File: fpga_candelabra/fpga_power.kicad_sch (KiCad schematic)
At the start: 1 part, among them U1 XCVU13P-B2104

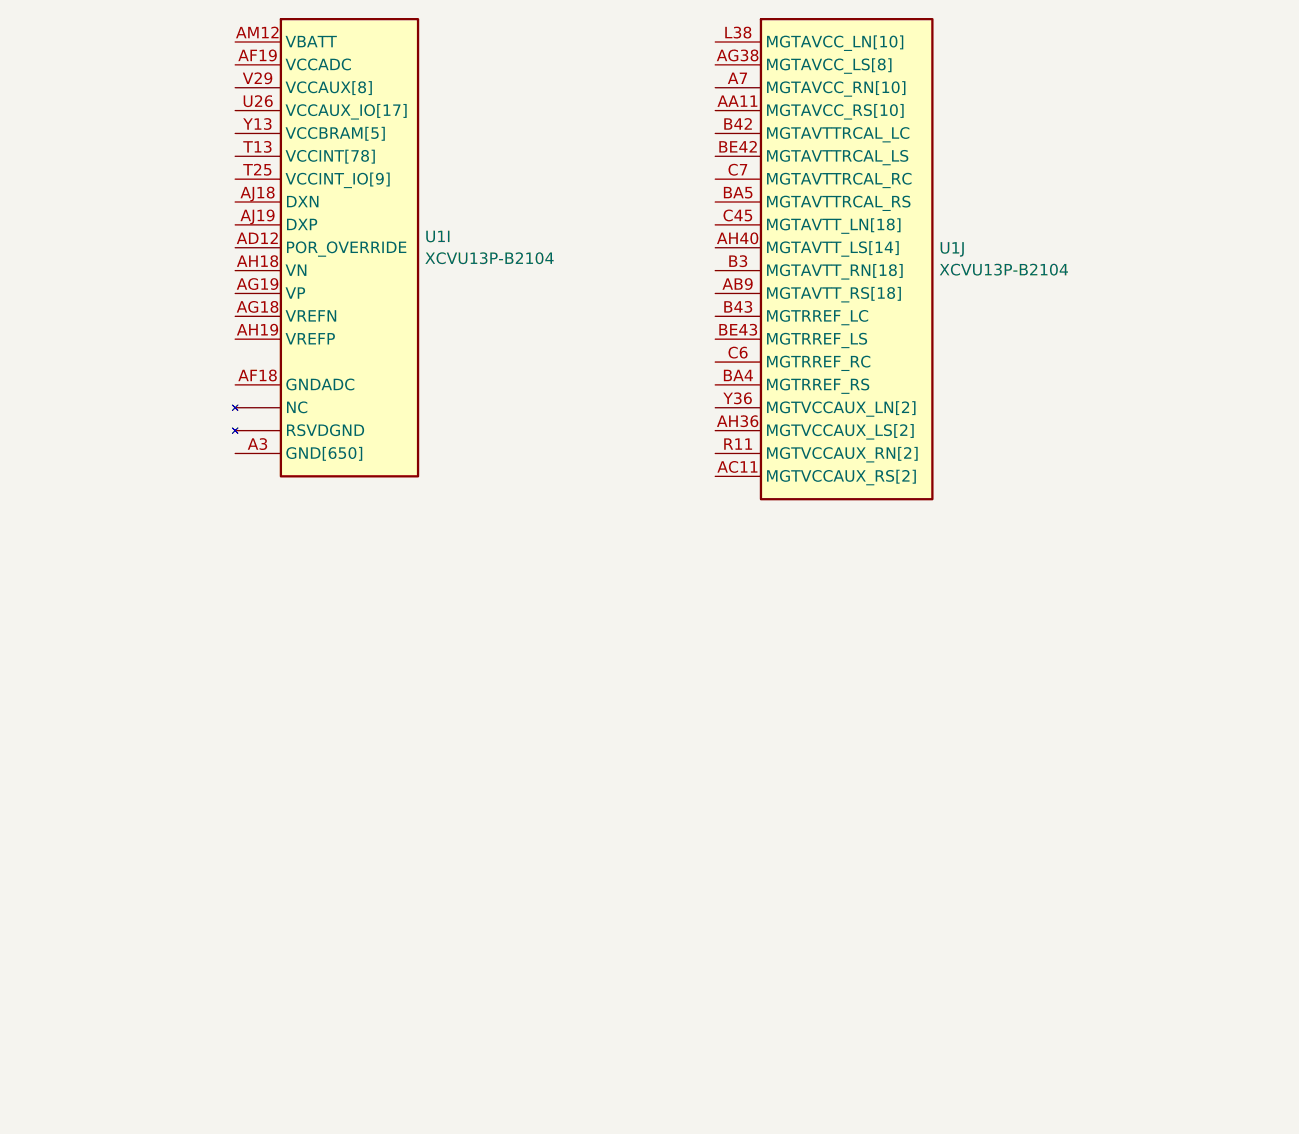
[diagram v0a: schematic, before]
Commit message: fpga_candelabra: add ddr4 power and sysmon mcu periph, bump library
Signed-off-by: Yichuan Gao <gaoyichuan000@gmail.com>
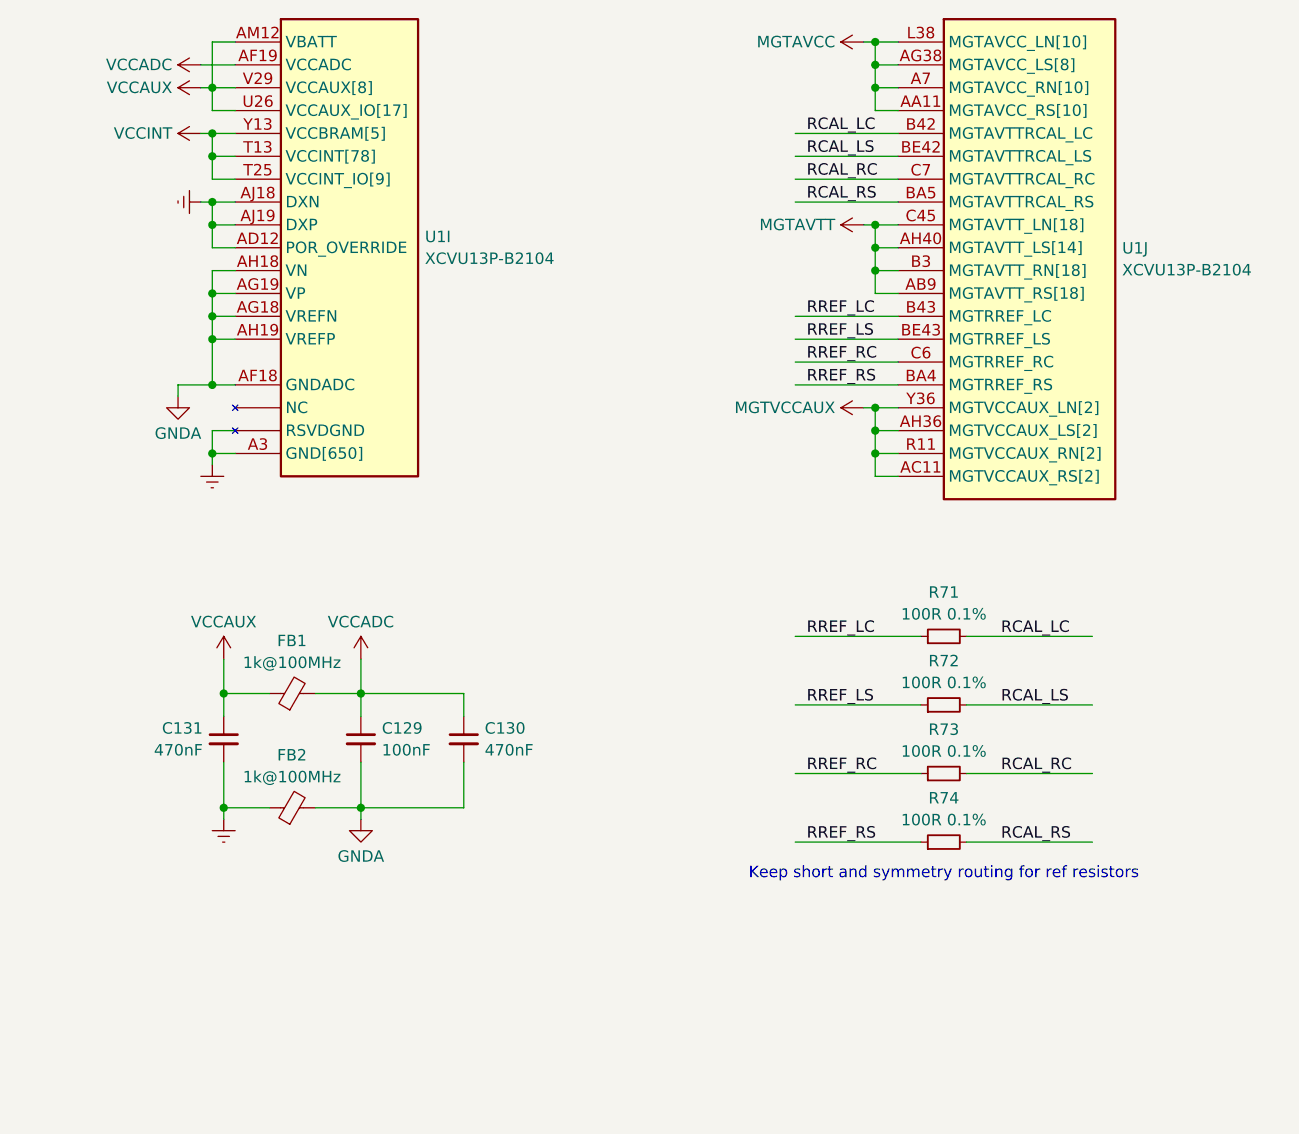
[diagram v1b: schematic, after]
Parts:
- added C129: 100nF, Capacitor_SMD:C_0402_1005Metric, symbol Device:C_Small
- added C130, C131: 470nF, Capacitor_SMD:C_0402_1005Metric, symbol Device:C_Small
- added FB1, FB2: 1k@100MHz, Inductor_SMD:L_0402_1005Metric, symbol Device:FerriteBead_Small
- added R71, R72, R73, R74: 100R 0.1%, Resistor_SMD:R_0402_1005Metric, symbol Device:R_Small
- U1: footprint (none) -> CHIPSAlliance_Package_BGA:Xilinx_FHGB2104_VU13P_PkgLength
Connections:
- net Earth: now reaches U1.A10 (GND[650]), U1.A12 (GND[650]), U1.A21 (GND[650]), U1.A3 (GND[650]), U1.A31 (GND[650]), U1.A41 (GND[650]), U1.A44 (GND[650]), U1.A6 (GND[650]), U1.AA1 (GND[650]), U1.AA10 (GND[650]), U1.AA13 (GND[650]), U1.AA15 (GND[650]), U1.AA17 (GND[650]), U1.AA19 (GND[650]), U1.AA2 (GND[650]), U1.AA21 (GND[650]), U1.AA23 (GND[650]), U1.AA25 (GND[650]), U1.AA27 (GND[650]), U1.AA29 (GND[650]), U1.AA31 (GND[650]), U1.AA35 (GND[650]), U1.AA38 (GND[650]), U1.AA42 (GND[650]), U1.AA43 (GND[650]), U1.AA44 (GND[650]), U1.AA5 (GND[650]), U1.AA6 (GND[650]), U1.AA7 (GND[650]), U1.AB12 (GND[650]), U1.AB14 (GND[650]), U1.AB16 (GND[650]), U1.AB18 (GND[650]), U1.AB20 (GND[650]), U1.AB22 (GND[650]), U1.AB24 (GND[650]), U1.AB26 (GND[650]), U1.AB28 (GND[650]), U1.AB3 (GND[650]), U1.AB30 (GND[650]), U1.AB35 (GND[650]), U1.AB37 (GND[650]), U1.AB4 (GND[650]), U1.AB40 (GND[650]), U1.AB42 (GND[650]), U1.AB45 (GND[650]), U1.AB46 (GND[650]), U1.AB5 (GND[650]), U1.AB8 (GND[650]), U1.AC1 (GND[650]), U1.AC10 (GND[650]), U1.AC15 (GND[650]), U1.AC17 (GND[650]), U1.AC19 (GND[650]), U1.AC2 (GND[650]), U1.AC21 (GND[650]), U1.AC23 (GND[650]), U1.AC25 (GND[650]), U1.AC27 (GND[650]), U1.AC29 (GND[650]), U1.AC35 (GND[650]), U1.AC39 (GND[650]), U1.AC42 (GND[650]), U1.AC43 (GND[650]), U1.AC44 (GND[650]), U1.AC5 (GND[650]), U1.AC7 (GND[650]), U1.AD14 (GND[650]), U1.AD16 (GND[650]), U1.AD18 (GND[650]), U1.AD20 (GND[650]), U1.AD22 (GND[650]), U1.AD24 (GND[650]), U1.AD26 (GND[650]), U1.AD28 (GND[650]), U1.AD3 (GND[650]), U1.AD32 (GND[650]), U1.AD35 (GND[650]), U1.AD37 (GND[650]), U1.AD4 (GND[650]), U1.AD41 (GND[650]), U1.AD42 (GND[650]), U1.AD45 (GND[650]), U1.AD46 (GND[650]), U1.AD5 (GND[650]), U1.AD9 (GND[650]), U1.AE1 (GND[650]), U1.AE10 (GND[650]), U1.AE17 (GND[650]), U1.AE19 (GND[650]), U1.AE2 (GND[650]), U1.AE21 (GND[650]), U1.AE23 (GND[650]), U1.AE25 (GND[650]), U1.AE27 (GND[650]), U1.AE29 (GND[650]), U1.AE35 (GND[650]), U1.AE38 (GND[650]), U1.AE42 (GND[650]), U1.AE43 (GND[650]), U1.AE44 (GND[650]), U1.AE5 (GND[650]), U1.AE6 (GND[650]), U1.AF12 (GND[650]), U1.AF14 (GND[650]), U1.AF16 (GND[650]), U1.AF20 (GND[650]), U1.AF22 (GND[650]), U1.AF24 (GND[650]), U1.AF26 (GND[650]), U1.AF28 (GND[650]), U1.AF3 (GND[650]), U1.AF35 (GND[650]), U1.AF36 (GND[650]), U1.AF4 (GND[650]), U1.AF40 (GND[650]), U1.AF42 (GND[650]), U1.AF45 (GND[650]), U1.AF46 (GND[650]), U1.AF5 (GND[650]), U1.AF8 (GND[650]), U1.AG1 (GND[650]), U1.AG11 (GND[650]), U1.AG17 (GND[650]), U1.AG2 (GND[650]), U1.AG21 (GND[650]), U1.AG23 (GND[650]), U1.AG25 (GND[650]), U1.AG27 (GND[650]), U1.AG33 (GND[650]), U1.AG35 (GND[650]), U1.AG39 (GND[650]), U1.AG42 (GND[650]), U1.AG43 (GND[650]), U1.AG44 (GND[650]), U1.AG5 (GND[650]), U1.AG7 (GND[650]), U1.AH14 (GND[650]), U1.AH16 (GND[650]), U1.AH20 (GND[650]), U1.AH22 (GND[650]), U1.AH24 (GND[650]), U1.AH26 (GND[650]), U1.AH3 (GND[650]), U1.AH30 (GND[650]), U1.AH35 (GND[650]), U1.AH37 (GND[650]), U1.AH4 (GND[650]), U1.AH41 (GND[650]), U1.AH42 (GND[650]), U1.AH45 (GND[650]), U1.AH46 (GND[650]), U1.AH5 (GND[650]), U1.AH9 (GND[650]), U1.AJ1 (GND[650]), U1.AJ10 (GND[650]), U1.AJ13 (GND[650]), U1.AJ15 (GND[650]), U1.AJ17 (GND[650]), U1.AJ2 (GND[650]), U1.AJ21 (GND[650]), U1.AJ23 (GND[650]), U1.AJ25 (GND[650]), U1.AJ35 (GND[650]), U1.AJ38 (GND[650]), U1.AJ42 (GND[650]), U1.AJ43 (GND[650]), U1.AJ44 (GND[650]), U1.AJ5 (GND[650]), U1.AJ6 (GND[650]), U1.AK14 (GND[650]), U1.AK16 (GND[650]), U1.AK18 (GND[650]), U1.AK20 (GND[650]), U1.AK22 (GND[650]), U1.AK24 (GND[650]), U1.AK3 (GND[650]), U1.AK34 (GND[650]), U1.AK35 (GND[650]), U1.AK37 (GND[650]), U1.AK4 (GND[650]), U1.AK40 (GND[650]), U1.AK42 (GND[650]), U1.AK45 (GND[650]), U1.AK46 (GND[650]), U1.AK5 (GND[650]), U1.AK8 (GND[650]), U1.AL1 (GND[650]), U1.AL11 (GND[650]), U1.AL2 (GND[650]), U1.AL31 (GND[650]), U1.AL35 (GND[650]), U1.AL39 (GND[650]), U1.AL42 (GND[650]), U1.AL43 (GND[650]), U1.AL44 (GND[650]), U1.AL5 (GND[650]), U1.AL7 (GND[650]), U1.AM18 (GND[650]), U1.AM28 (GND[650]), U1.AM3 (GND[650]), U1.AM35 (GND[650]), U1.AM37 (GND[650]), U1.AM4 (GND[650]), U1.AM41 (GND[650]), U1.AM42 (GND[650]), U1.AM45 (GND[650]), U1.AM46 (GND[650]), U1.AM5 (GND[650]), U1.AM9 (GND[650]), U1.AN1 (GND[650]), U1.AN10 (GND[650]), U1.AN12 (GND[650]), U1.AN15 (GND[650]), U1.AN2 (GND[650]), U1.AN25 (GND[650]), U1.AN35 (GND[650]), U1.AN38 (GND[650]), U1.AN42 (GND[650]), U1.AN43 (GND[650]), U1.AN44 (GND[650]), U1.AN5 (GND[650]), U1.AN6 (GND[650]), U1.AP12 (GND[650]), U1.AP22 (GND[650]), U1.AP3 (GND[650]), U1.AP32 (GND[650]), U1.AP35 (GND[650]), U1.AP36 (GND[650]), U1.AP4 (GND[650]), U1.AP40 (GND[650]), U1.AP42 (GND[650]), U1.AP45 (GND[650]), U1.AP46 (GND[650]), U1.AP5 (GND[650]), U1.AP8 (GND[650]), U1.AR1 (GND[650]), U1.AR11 (GND[650]), U1.AR12 (GND[650]), U1.AR19 (GND[650]), U1.AR2 (GND[650]), U1.AR29 (GND[650]), U1.AR35 (GND[650]), U1.AR39 (GND[650]), U1.AR42 (GND[650]), U1.AR43 (GND[650]), U1.AR44 (GND[650]), U1.AR5 (GND[650]), U1.AR7 (GND[650]), U1.AT12 (GND[650]), U1.AT16 (GND[650]), U1.AT26 (GND[650]), U1.AT3 (GND[650]), U1.AT35 (GND[650]), U1.AT37 (GND[650]), U1.AT4 (GND[650]), U1.AT41 (GND[650]), U1.AT42 (GND[650]), U1.AT45 (GND[650]), U1.AT46 (GND[650]), U1.AT5 (GND[650]), U1.AT9 (GND[650]), U1.AU1 (GND[650]), U1.AU10 (GND[650]), U1.AU12 (GND[650]), U1.AU2 (GND[650]), U1.AU23 (GND[650]), U1.AU33 (GND[650]), U1.AU35 (GND[650]), U1.AU38 (GND[650]), U1.AU42 (GND[650]), U1.AU43 (GND[650]), U1.AU44 (GND[650]), U1.AU5 (GND[650]), U1.AU6 (GND[650]), U1.AV12 (GND[650]), U1.AV20 (GND[650]), U1.AV3 (GND[650]), U1.AV30 (GND[650]), U1.AV35 (GND[650]), U1.AV36 (GND[650]), U1.AV37 (GND[650]), U1.AV4 (GND[650]), U1.AV40 (GND[650]), U1.AV42 (GND[650]), U1.AV45 (GND[650]), U1.AV46 (GND[650]), U1.AV5 (GND[650]), U1.AV8 (GND[650]), U1.AW1 (GND[650]), U1.AW10 (GND[650]), U1.AW11 (GND[650]), U1.AW12 (GND[650]), U1.AW17 (GND[650]), U1.AW2 (GND[650]), U1.AW27 (GND[650]), U1.AW37 (GND[650]), U1.AW39 (GND[650]), U1.AW42 (GND[650]), U1.AW43 (GND[650]), U1.AW44 (GND[650]), U1.AW5 (GND[650]), U1.AW6 (GND[650]), U1.AY1 (GND[650]), U1.AY10 (GND[650]), U1.AY14 (GND[650]), U1.AY2 (GND[650]), U1.AY24 (GND[650]), U1.AY3 (GND[650]), U1.AY34 (GND[650]), U1.AY37 (GND[650]), U1.AY4 (GND[650]), U1.AY41 (GND[650]), U1.AY42 (GND[650]), U1.AY43 (GND[650]), U1.AY44 (GND[650]), U1.AY45 (GND[650]), U1.AY46 (GND[650]), U1.AY5 (GND[650]), U1.AY6 (GND[650]), U1.AY7 (GND[650]), U1.AY8 (GND[650]), U1.AY9 (GND[650]), U1.B12 (GND[650]), U1.B18 (GND[650]), U1.B2 (GND[650]), U1.B28 (GND[650]), U1.B38 (GND[650]), U1.B4 (GND[650]), U1.B41 (GND[650]), U1.B44 (GND[650]), U1.B45 (GND[650]), U1.B5 (GND[650]), U1.B6 (GND[650]), U1.B7 (GND[650]), U1.B8 (GND[650]), U1.BA11 (GND[650]), U1.BA21 (GND[650]), U1.BA3 (GND[650]), U1.BA31 (GND[650]), U1.BA37 (GND[650]), U1.BA38 (GND[650]), U1.BA39 (GND[650]), U1.BA44 (GND[650]), U1.BA6 (GND[650]), U1.BB1 (GND[650]), U1.BB18 (GND[650]), U1.BB2 (GND[650]), U1.BB28 (GND[650]), U1.BB3 (GND[650]), U1.BB39 (GND[650]), U1.BB40 (GND[650]), U1.BB41 (GND[650]), U1.BB44 (GND[650]), U1.BB45 (GND[650]), U1.BB46 (GND[650]), U1.BB6 (GND[650]), U1.BB8 (GND[650]), U1.BC15 (GND[650]), U1.BC25 (GND[650]), U1.BC3 (GND[650]), U1.BC35 (GND[650]), U1.BC4 (GND[650]), U1.BC41 (GND[650]), U1.BC42 (GND[650]), U1.BC44 (GND[650]), U1.BC6 (GND[650]), U1.BD1 (GND[650]), U1.BD12 (GND[650]), U1.BD22 (GND[650]), U1.BD3 (GND[650]), U1.BD32 (GND[650]), U1.BD41 (GND[650]), U1.BD44 (GND[650]), U1.BD46 (GND[650]), U1.BD6 (GND[650]), U1.BE19 (GND[650]), U1.BE2 (GND[650]), U1.BE29 (GND[650]), U1.BE3 (GND[650]), U1.BE39 (GND[650]), U1.BE41 (GND[650]), U1.BE45 (GND[650]), U1.BE5 (GND[650]), U1.BE6 (GND[650]), U1.BE9 (GND[650]), U1.BF16 (GND[650]), U1.BF26 (GND[650]), U1.BF3 (GND[650]), U1.BF36 (GND[650]), U1.BF41 (GND[650]), U1.BF44 (GND[650]), U1.BF6 (GND[650]), U1.C1 (GND[650]), U1.C11 (GND[650]), U1.C12 (GND[650]), U1.C15 (GND[650]), U1.C2 (GND[650]), U1.C25 (GND[650]), U1.C35 (GND[650])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
- net Earth: now also U1.AD12 (POR_OVERRIDE), U1.AJ18 (DXN), U1.AJ19 (DXP), U1.W12 (RSVDGND), C131.2, FB2.1
- net VCCINT: now reaches U1.AA14 (VCCINT[78]), U1.AA16 (VCCINT[78]), U1.AA18 (VCCINT[78]), U1.AA20 (VCCINT[78]), U1.AA22 (VCCINT[78]), U1.AA24 (VCCINT[78]), U1.AB15 (VCCINT[78]), U1.AB17 (VCCINT[78]), U1.AB19 (VCCINT[78]), U1.AB21 (VCCINT[78]), U1.AB23 (VCCINT[78]), U1.AC16 (VCCINT[78]), U1.AC18 (VCCINT[78]), U1.AC20 (VCCINT[78]), U1.AC22 (VCCINT[78]), U1.AD15 (VCCINT[78]), U1.AD17 (VCCINT[78]), U1.AD19 (VCCINT[78]), U1.AD21 (VCCINT[78]), U1.AD23 (VCCINT[78]), U1.AE16 (VCCINT[78]), U1.AE18 (VCCINT[78]), U1.AE20 (VCCINT[78]), U1.AE22 (VCCINT[78]), U1.AE24 (VCCINT[78]), U1.AF15 (VCCINT[78]), U1.AF17 (VCCINT[78]), U1.AF21 (VCCINT[78]), U1.AF23 (VCCINT[78]), U1.AG16 (VCCINT[78]), U1.AG20 (VCCINT[78]), U1.AG22 (VCCINT[78]), U1.AG24 (VCCINT[78]), U1.AH13 (VCCINT[78]), U1.AH15 (VCCINT[78]), U1.AH17 (VCCINT[78]), U1.AH21 (VCCINT[78]), U1.AH23 (VCCINT[78]), U1.AJ14 (VCCINT[78]), U1.AJ16 (VCCINT[78]), U1.AJ20 (VCCINT[78]), U1.AJ22 (VCCINT[78]), U1.AJ24 (VCCINT[78]), U1.AK13 (VCCINT[78]), U1.AK15 (VCCINT[78]), U1.AK17 (VCCINT[78]), U1.AK19 (VCCINT[78]), U1.AK21 (VCCINT[78]), U1.AK23 (VCCINT[78]), U1.T13 (VCCINT[78]), U1.T15 (VCCINT[78]), U1.T17 (VCCINT[78]), U1.T19 (VCCINT[78]), U1.T21 (VCCINT[78]), U1.T23 (VCCINT[78]), U1.U14 (VCCINT[78]), U1.U16 (VCCINT[78]), U1.U18 (VCCINT[78]), U1.U20 (VCCINT[78]), U1.U22 (VCCINT[78]), U1.U24 (VCCINT[78]), U1.V13 (VCCINT[78]), U1.V15 (VCCINT[78]), U1.V17 (VCCINT[78]), U1.V19 (VCCINT[78]), U1.V21 (VCCINT[78]), U1.V23 (VCCINT[78]), U1.W14 (VCCINT[78]), U1.W16 (VCCINT[78]), U1.W18 (VCCINT[78]), U1.W20 (VCCINT[78]), U1.W22 (VCCINT[78]), U1.W24 (VCCINT[78]), U1.Y15 (VCCINT[78]), U1.Y17 (VCCINT[78]), U1.Y19 (VCCINT[78]), U1.Y21 (VCCINT[78]), U1.Y23 (VCCINT[78])
- net VCCINT: now also U1.AB13 (VCCBRAM[5]), U1.AB25 (VCCINT_IO[9]), U1.AC14 (VCCBRAM[5]), U1.AC24 (VCCINT_IO[9]), U1.AD25 (VCCINT_IO[9]), U1.AE14 (VCCBRAM[5]), U1.AE26 (VCCINT_IO[9]), U1.AF25 (VCCINT_IO[9]), U1.AG14 (VCCBRAM[5]), U1.AH25 (VCCINT_IO[9]), U1.T25 (VCCINT_IO[9]), U1.V25 (VCCINT_IO[9]), U1.Y13 (VCCBRAM[5]), U1.Y25 (VCCINT_IO[9])
- net VCCAUX: now reaches U1.AA26 (VCCAUX_IO[17]), U1.AA28 (VCCAUX_IO[17]), U1.AB27 (VCCAUX_IO[17]), U1.AC26 (VCCAUX_IO[17]), U1.AC28 (VCCAUX_IO[17]), U1.AD27 (VCCAUX_IO[17]), U1.AE28 (VCCAUX_IO[17]), U1.AF27 (VCCAUX_IO[17]), U1.AG26 (VCCAUX_IO[17]), U1.AG28 (VCCAUX_IO[17]), U1.AH27 (VCCAUX_IO[17]), U1.AJ26 (VCCAUX_IO[17]), U1.U26 (VCCAUX_IO[17]), U1.U28 (VCCAUX_IO[17]), U1.V27 (VCCAUX_IO[17]), U1.W26 (VCCAUX_IO[17]), U1.Y27 (VCCAUX_IO[17])
- net VCCAUX: now also U1.AA30 (VCCAUX[8]), U1.AB29 (VCCAUX[8]), U1.AC30 (VCCAUX[8]), U1.AD29 (VCCAUX[8]), U1.AF29 (VCCAUX[8]), U1.AM12 (VBATT), U1.V29 (VCCAUX[8]), U1.W28 (VCCAUX[8]), U1.Y29 (VCCAUX[8]), C131.1, FB1.1
- net GNDA: now reaches U1.AF18 (GNDADC)
- net GNDA: now also U1.AG18 (VREFN), U1.AG19 (VP), U1.AH18 (VN), U1.AH19 (VREFP), C129.2, C130.2, FB2.2
- net VCCADC: now reaches U1.AF19 (VCCADC)
- net VCCADC: now also C129.1, C130.1, FB1.2
- net MGTAVCC: now reaches U1.A11 (MGTAVCC_RN[10]), U1.A7 (MGTAVCC_RN[10]), U1.B9 (MGTAVCC_RN[10]), U1.C10 (MGTAVCC_RN[10]), U1.E11 (MGTAVCC_RN[10]), U1.G10 (MGTAVCC_RN[10]), U1.J11 (MGTAVCC_RN[10]), U1.L10 (MGTAVCC_RN[10]), U1.N11 (MGTAVCC_RN[10]), U1.W10 (MGTAVCC_RN[10])
- net MGTAVCC: now also U1.AA11 (MGTAVCC_RS[10]), U1.AD36 (MGTAVCC_LN[10]), U1.AF37 (MGTAVCC_LN[10]), U1.AG10 (MGTAVCC_RS[10]), U1.AG38 (MGTAVCC_LS[8]), U1.AJ11 (MGTAVCC_RS[10]), U1.AL10 (MGTAVCC_RS[10]), U1.AL38 (MGTAVCC_LS[8]), U1.AM36 (MGTAVCC_LS[8]), U1.AN11 (MGTAVCC_RS[10]), U1.AP37 (MGTAVCC_LS[8]), U1.AP9 (MGTAVCC_RS[10]), U1.AR10 (MGTAVCC_RS[10]), U1.AR38 (MGTAVCC_LS[8]), U1.AT36 (MGTAVCC_LS[8]), U1.AU11 (MGTAVCC_RS[10]), U1.AV9 (MGTAVCC_RS[10]), U1.AW38 (MGTAVCC_LS[8]), U1.AW7 (MGTAVCC_RS[10]), U1.AY40 (MGTAVCC_LS[8]), U1.L38 (MGTAVCC_LN[10]), U1.M36 (MGTAVCC_LN[10]), U1.N39 (MGTAVCC_LN[10]), U1.P37 (MGTAVCC_LN[10]), U1.R38 (MGTAVCC_LN[10]), U1.T36 (MGTAVCC_LN[10]), U1.U39 (MGTAVCC_LN[10]), U1.V37 (MGTAVCC_LN[10])
- net MGTAVTT: now reaches U1.AA39 (MGTAVTT_LN[18]), U1.AB41 (MGTAVTT_LN[18]), U1.AC38 (MGTAVTT_LN[18]), U1.AD40 (MGTAVTT_LN[18]), U1.AE39 (MGTAVTT_LN[18]), U1.AF41 (MGTAVTT_LN[18]), U1.C45 (MGTAVTT_LN[18]), U1.D43 (MGTAVTT_LN[18]), U1.F42 (MGTAVTT_LN[18]), U1.F43 (MGTAVTT_LN[18]), U1.H40 (MGTAVTT_LN[18]), U1.K41 (MGTAVTT_LN[18]), U1.M40 (MGTAVTT_LN[18]), U1.P41 (MGTAVTT_LN[18]), U1.T40 (MGTAVTT_LN[18]), U1.V41 (MGTAVTT_LN[18]), U1.W38 (MGTAVTT_LN[18]), U1.Y40 (MGTAVTT_LN[18])
- net MGTAVTT: now also U1.AB9 (MGTAVTT_RS[18]), U1.AC6 (MGTAVTT_RS[18]), U1.AD8 (MGTAVTT_RS[18]), U1.AE7 (MGTAVTT_RS[18]), U1.AF9 (MGTAVTT_RS[18]), U1.AG6 (MGTAVTT_RS[18]), U1.AH40 (MGTAVTT_LS[14]), U1.AH8 (MGTAVTT_RS[18]), U1.AJ39 (MGTAVTT_LS[14]), U1.AJ7 (MGTAVTT_RS[18]), U1.AK41 (MGTAVTT_LS[14]), U1.AK9 (MGTAVTT_RS[18]), U1.AL6 (MGTAVTT_RS[18]), U1.AM40 (MGTAVTT_LS[14]), U1.AM8 (MGTAVTT_RS[18]), U1.AN39 (MGTAVTT_LS[14]), U1.AN7 (MGTAVTT_RS[18]), U1.AP41 (MGTAVTT_LS[14]), U1.AR6 (MGTAVTT_RS[18]), U1.AT40 (MGTAVTT_LS[14]), U1.AT8 (MGTAVTT_RS[18]), U1.AU39 (MGTAVTT_LS[14]), U1.AU7 (MGTAVTT_RS[18]), U1.AV41 (MGTAVTT_LS[14]), U1.B3 (MGTAVTT_RN[18]), U1.BA42 (MGTAVTT_LS[14]), U1.BA43 (MGTAVTT_LS[14]), U1.BC43 (MGTAVTT_LS[14]), U1.BC5 (MGTAVTT_RS[18]), U1.BD2 (MGTAVTT_RS[18]), U1.BD45 (MGTAVTT_LS[14]), U1.BE4 (MGTAVTT_RS[18]), U1.BE44 (MGTAVTT_LS[14]), U1.D8 (MGTAVTT_RN[18]), U1.E7 (MGTAVTT_RN[18]), U1.F9 (MGTAVTT_RN[18]), U1.G6 (MGTAVTT_RN[18]), U1.H8 (MGTAVTT_RN[18]), U1.J7 (MGTAVTT_RN[18]), U1.K9 (MGTAVTT_RN[18]), U1.L6 (MGTAVTT_RN[18]), U1.M8 (MGTAVTT_RN[18]), U1.N7 (MGTAVTT_RN[18]), U1.P9 (MGTAVTT_RN[18]), U1.R6 (MGTAVTT_RN[18]), U1.T8 (MGTAVTT_RN[18]), U1.U7 (MGTAVTT_RN[18]), U1.V9 (MGTAVTT_RN[18]), U1.W6 (MGTAVTT_RN[18]), U1.Y8 (MGTAVTT_RN[18])
- net MGTVCCAUX: now reaches U1.AB36 (MGTVCCAUX_LN[2]), U1.Y36 (MGTVCCAUX_LN[2])
- net MGTVCCAUX: now also U1.AC11 (MGTVCCAUX_RS[2]), U1.AE11 (MGTVCCAUX_RS[2]), U1.AH36 (MGTVCCAUX_LS[2]), U1.AK36 (MGTVCCAUX_LS[2]), U1.R11 (MGTVCCAUX_RN[2]), U1.U11 (MGTVCCAUX_RN[2])
- net RCAL_LC: now reaches U1.B42 (MGTAVTTRCAL_LC)
- net RCAL_LC: now also R71.2
- net RREF_LC: now reaches U1.B43 (MGTRREF_LC)
- net RREF_LC: now also R71.1
- net RREF_RS: now reaches U1.BA4 (MGTRREF_RS)
- net RREF_RS: now also R74.1
- net RCAL_RS: now reaches U1.BA5 (MGTAVTTRCAL_RS)
- net RCAL_RS: now also R74.2
- net RCAL_LS: now reaches U1.BE42 (MGTAVTTRCAL_LS)
- net RCAL_LS: now also R72.2
- net RREF_LS: now reaches U1.BE43 (MGTRREF_LS)
- net RREF_LS: now also R72.1
- net RREF_RC: now reaches U1.C6 (MGTRREF_RC)
- net RREF_RC: now also R73.1
- net RCAL_RC: now reaches U1.C7 (MGTAVTTRCAL_RC)
- net RCAL_RC: now also R73.2
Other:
- note added: "Keep short and symmetry routing for ref resistors"
- title: (none) -> FPGA Power Pins
- moved on the sheet: U1J

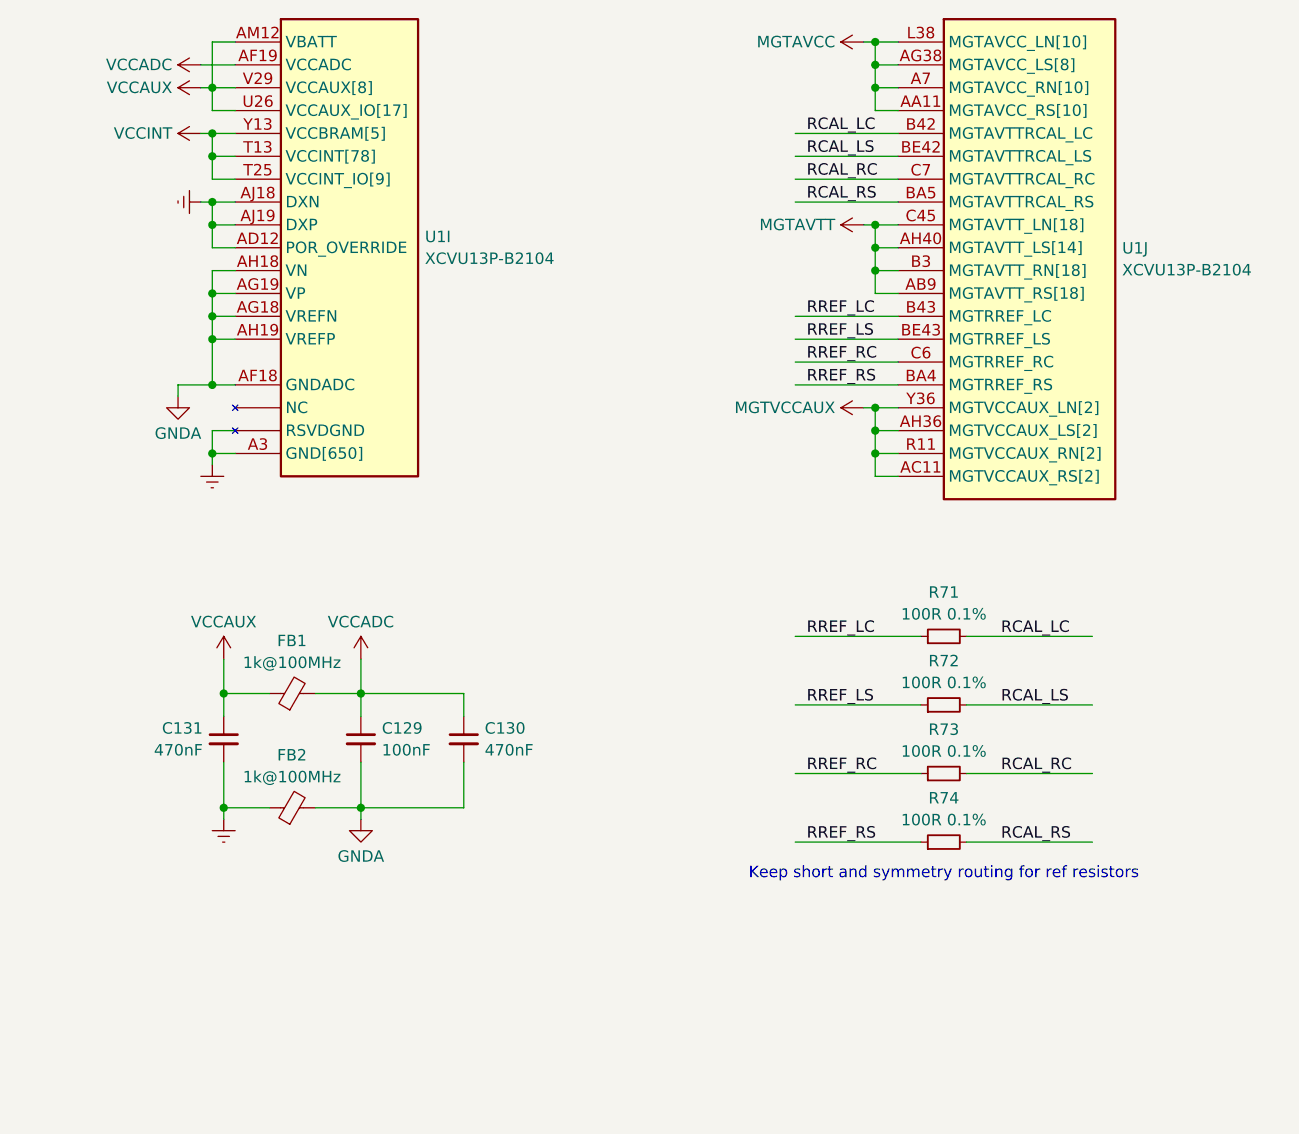
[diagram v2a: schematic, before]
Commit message: fpga_candelabra: sch & layout v0.5, pass basic ERC & DRC
Signed-off-by: Yichuan Gao <gaoyichuan000@gmail.com>
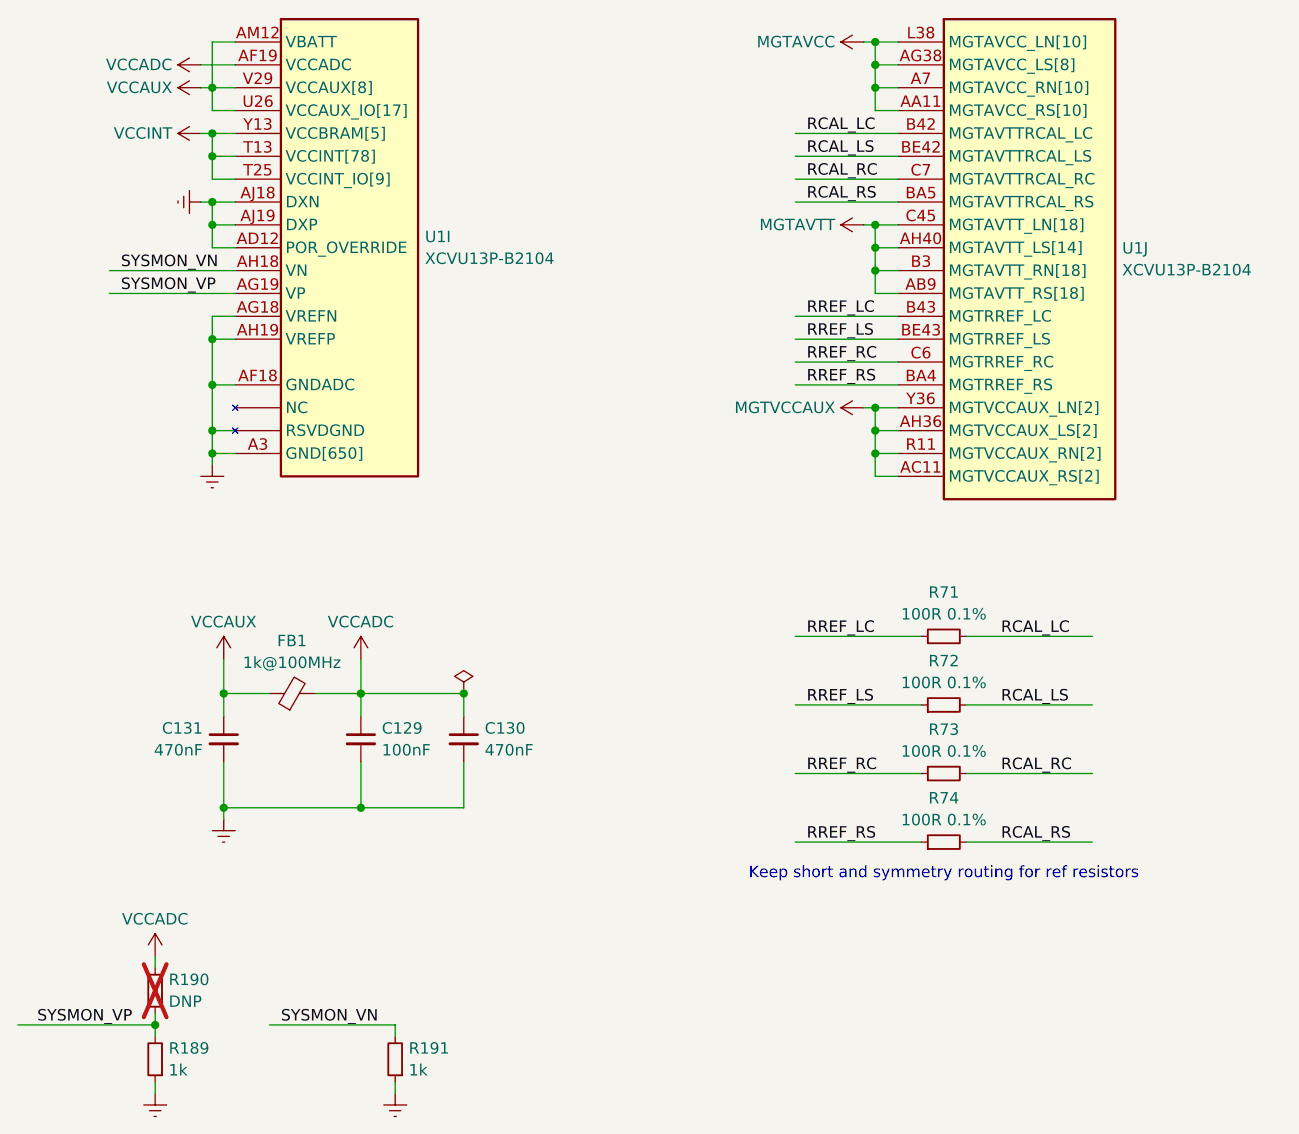
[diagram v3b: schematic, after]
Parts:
- removed FB2: 1k@100MHz, Inductor_SMD:L_0402_1005Metric, symbol Device:FerriteBead_Small
- added R189, R191: 1k, Resistor_SMD:R_0402_1005Metric, symbol Device:R_Small
- added R190: DNP, Resistor_SMD:R_0402_1005Metric, symbol Device:R_Small
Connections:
- net Earth: now also C129.2, C130.2, U1.AF18 (GNDADC), U1.AG18 (VREFN), U1.AH19 (VREFP), R189.1, R191.1
- net VCCADC: now also R190.2
- removed net GNDA: C129.2, C130.2, U1.AF18 (GNDADC), U1.AG18 (VREFN), U1.AG19 (VP), U1.AH18 (VN), U1.AH19 (VREFP)
- new net SYSMON_VN: R191.2, U1.AH18 (VN)
- new net SYSMON_VP: R189.2, R190.1, U1.AG19 (VP)

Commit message: fpga_candelabra: more bugfixes & improvements for rev 0.2.0
- Add Digilent JTAG-SMT2-NC onboard
- Add fan controller & 4pin fan header
- Use 9pin header for USB2.0
- Misc fixes for structure

Signed-off-by: Yichuan Gao <gaoyichuan000@gmail.com>
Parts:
- R72, R73, R74: LCSC Part C490806 -> C478864
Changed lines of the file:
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@@
 	(label "RCAL_RS"
 		(at 107.95 67.31 0)
-		(fields_autoplaced yes)
 		(effects
 			(font
@@
 	(label "RREF_RC"
 		(at 107.95 130.81 0)
-		(fields_autoplaced yes)
 		(effects
 			(font
@@
 	(label "SYSMON_VN"
 		(at 31.75 74.93 0)
-		(fields_autoplaced yes)
 		(effects
 			(font
@@
 	(label "SYSMON_VP"
 		(at 31.75 77.47 0)
-		(fields_autoplaced yes)
 		(effects
 			(font
@@
 	(label "RCAL_RS"
 		(at 129.54 138.43 0)
-		(fields_autoplaced yes)
 		(effects
 			(font
@@
 	(label "RREF_LC"
 		(at 107.95 115.57 0)
-		(fields_autoplaced yes)
 		(effects
 			(font
@@
 	(label "RCAL_LC"
 		(at 107.95 59.69 0)
-		(fields_autoplaced yes)
 		(effects
 			(font
@@
 	(label "RREF_RS"
 		(at 107.95 87.63 0)
-		(fields_autoplaced yes)
 		(effects
 			(font
@@
 	(label "RCAL_RC"
 		(at 107.95 64.77 0)
-		(fields_autoplaced yes)
 		(effects
 			(font
@@
 	(label "SYSMON_VN"
 		(at 49.53 158.75 0)
-		(fields_autoplaced yes)
 		(effects
 			(font
@@
 	(label "RREF_RS"
 		(at 107.95 138.43 0)
-		(fields_autoplaced yes)
 		(effects
 			(font
@@
 	(label "RCAL_LS"
 		(at 129.54 123.19 0)
-		(fields_autoplaced yes)
 		(effects
 			(font
@@
 	(label "RREF_LS"
 		(at 107.95 123.19 0)
-		(fields_autoplaced yes)
 		(effects
 			(font
@@
 	(label "RCAL_LS"
 		(at 107.95 62.23 0)
-		(fields_autoplaced yes)
 		(effects
 			(font
@@
 	(label "RREF_LC"
 		(at 107.95 80.01 0)
-		(fields_autoplaced yes)
 		(effects
 			(font
@@
 	(label "RCAL_RC"
 		(at 129.54 130.81 0)
-		(fields_autoplaced yes)
 		(effects
 			(font
@@
 	(label "RREF_LS"
 		(at 107.95 82.55 0)
-		(fields_autoplaced yes)
 		(effects
 			(font
@@
 	(label "SYSMON_VP"
 		(at 33.02 158.75 180)
-		(fields_autoplaced yes)
 		(effects
 			(font
@@
 	(label "RREF_RC"
 		(at 107.95 85.09 0)
-		(fields_autoplaced yes)
 		(effects
 			(font
@@
 	(label "RCAL_LC"
 		(at 129.54 115.57 0)
-		(fields_autoplaced yes)
 		(effects
 			(font
@@
 			)
 		)
-		(property "LCSC Part" "C490806"
+		(property "LCSC Part" "C478864"
 			(at 123.19 123.19 0)
 			(effects
@@
 			)
 		)
-		(property "LCSC Part" "C490806"
+		(property "LCSC Part" "C478864"
 			(at 123.19 130.81 0)
 			(effects
@@
 			)
 		)
-		(property "LCSC Part" "C490806"
+		(property "LCSC Part" "C478864"
 			(at 123.19 138.43 0)
 			(effects

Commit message: fpga_candelabra: add author & rev to schematics
Signed-off-by: Yichuan Gao <gaoyichuan000@gmail.com>
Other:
- company: (none) -> CHIPS Alliance
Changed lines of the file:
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@@
 	(title_block
 		(title "FPGA Power Pins")
+		(date "2025-02-05")
+		(rev "0.2.0")
+		(company "CHIPS Alliance")
+		(comment 1 "Yichuan Gao")
+		(comment 2 "Yichuan Gao")
 	)
 	(junction

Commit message: fpga_candelabra: update to kicad 9.0
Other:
- company: CHIPS Alliance -> Sipeed
